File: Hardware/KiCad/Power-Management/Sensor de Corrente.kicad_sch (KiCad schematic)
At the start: 4 parts, among them U2 ACS758xCB-050B-PFF

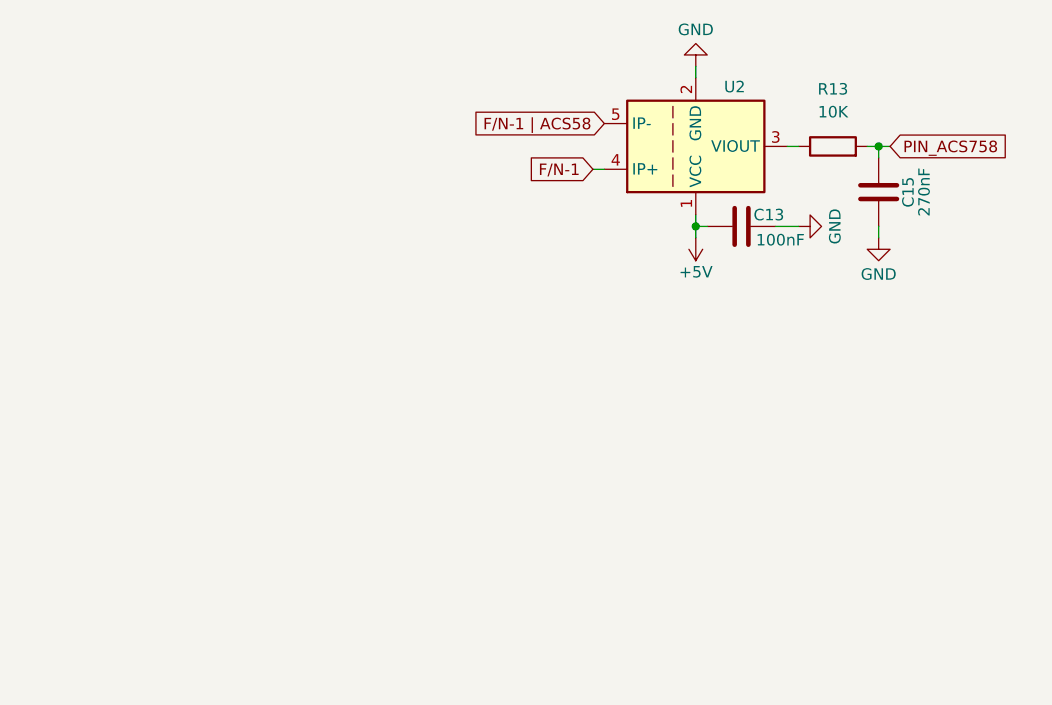
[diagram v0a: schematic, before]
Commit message: troca de sensor de corrente
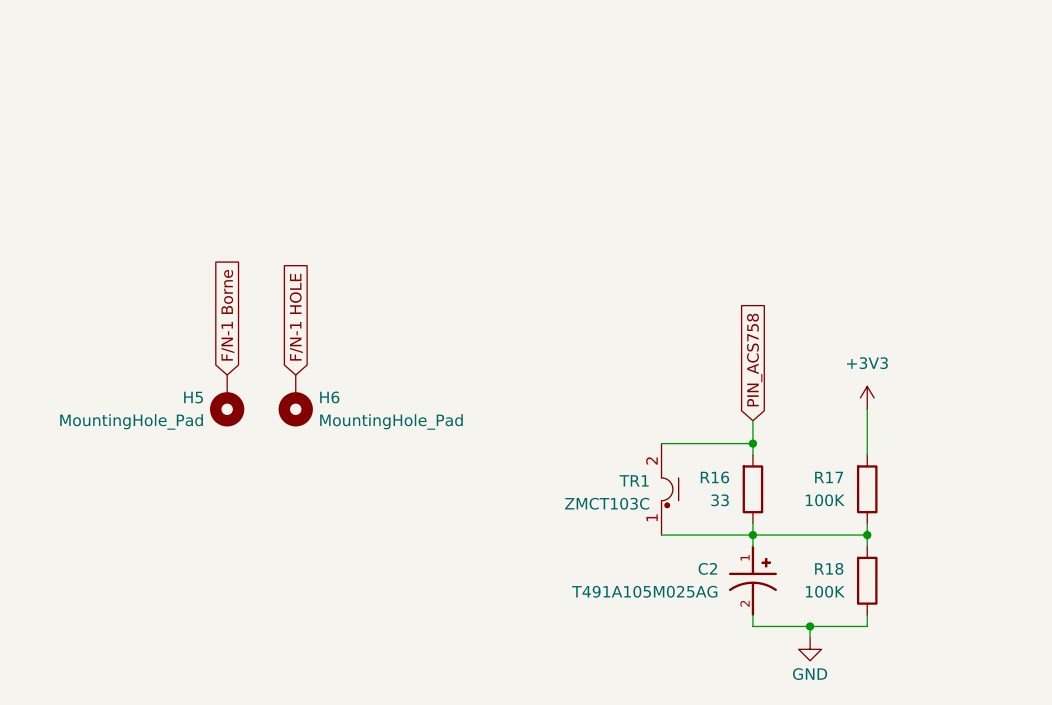
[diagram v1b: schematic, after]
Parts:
- removed C13: 100nF, Capacitor_SMD:C_0805_2012Metric_Pad1.18x1.45mm_HandSolder, symbol Device:C
- removed C15: 270nF, Capacitor_SMD:C_0805_2012Metric_Pad1.18x1.45mm_HandSolder, symbol Device:C
- removed R13: 10K, Resistor_SMD:R_0805_2012Metric_Pad1.20x1.40mm_HandSolder, symbol Device:R
- removed U2: ACS758xCB-050B-PFF, Sensor_Current:Allegro_CB_PFF, symbol Sensor_Current:ACS758xCB-050B-PFF
- added C2: T491A105M025AG, T491A105M025AG:CAPMP3216X180N, symbol T491A105M025AG:T491A105M025AG
- added H5, H6: MountingHole_Pad, MountingHole:MountingHole_2.2mm_M2_Pad_Via, symbol Mechanical:MountingHole_Pad
- added R16: 33, Resistor_SMD:R_0805_2012Metric_Pad1.20x1.40mm_HandSolder, symbol Device:R
- added R17, R18: 100K, Resistor_SMD:R_0805_2012Metric_Pad1.20x1.40mm_HandSolder, symbol Device:R
- added TR1: ZMCT103C, Transformer_THT:Transformer_Zeming_ZMCT103C, symbol Transformer:ZMCT103C
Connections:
- net GND: now also C2.2, R18.1
- net PIN_ACS758: now also R16.2, TR1.2
- new net: C2.1, R16.1, R17.1, R18.2, TR1.1
- new net +3V3: R17.2
- new net F/N-1 Borne: H5.1
- new net F/N-1 HOLE: H6.1
